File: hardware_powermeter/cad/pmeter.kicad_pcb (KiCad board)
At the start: 4 copper layers, 47 x 14 mm, 59 parts, among them J101 conector magnetico 6 vias, J102 furos da celula, J301 furos da ponte, U101 nPM1100-QDAB, U102 MAX17048G+T10, U201 HOLYIOT-26001-A, U301 ADS1220IRVAR, U302 TPS22916BYFPR, U401 BMA400, U402 TMP117AIDRVR

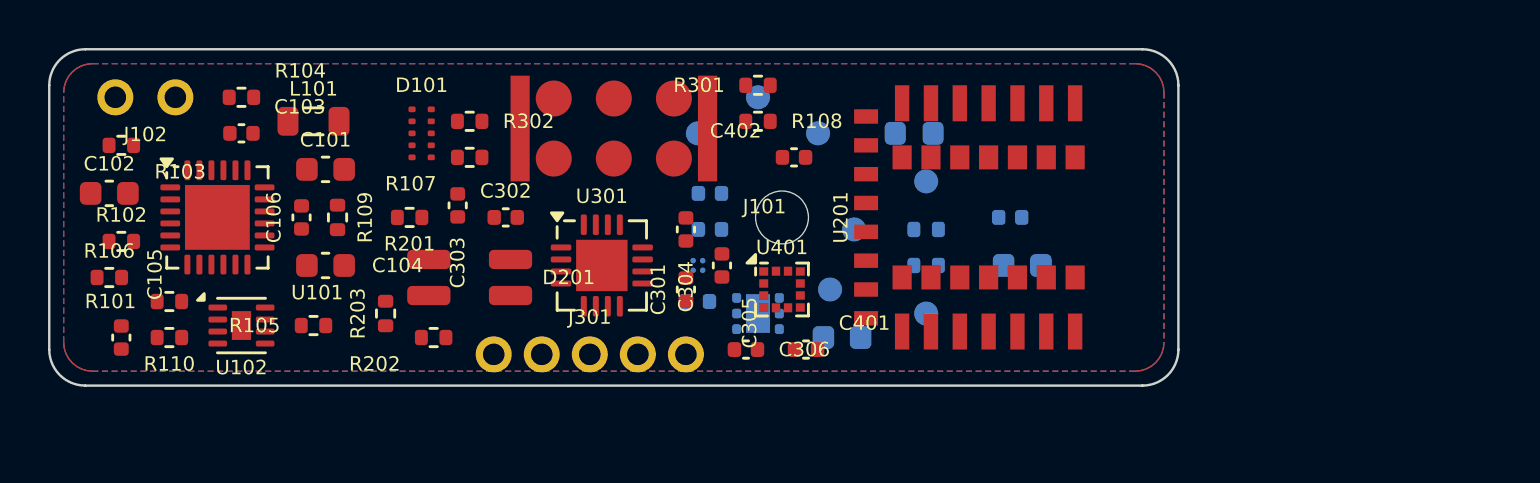
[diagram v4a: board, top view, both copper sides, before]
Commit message: feat(hardware): the board routed with zero DRC errors, and every view redrawn
The chain ran in its documented order for the first time since the module
swap -- make_pcb, route, fill_zones, drc, reparar, twice -- and the board
came out with 440 segments, 153 vias, 75 connections and NO DRC errors.
The 25 warnings are all library registration: the footprints here are
generated, not taken from a registered library.

What is still open, and the board cannot be fabricated until it closes:
three signal connections with no copper (I2C_SCL, SPI_MOSI, SPI_SCK, all
in the same stretch between the converter and the module), and seven of
seventeen decoupling capacitors past the datasheet limit. The second one
was measured from inside the placer rather than guessed: it decides
correctly, and the nearest FREE slot really is 2,90 mm from C302's pin.
What eats that radius is the stack of courtyards, so on a 3,5 mm VQFN
with a 0402 on the same face the datasheet's 2 mm may not fit at all.

The negotiated-congestion stage ran all 160 rounds and was refused: it
reaches zero contested cells only at 62 to 64 connections against the
sequential 75, and the criterion wants both.

Dry runs: 14 rules met on the board, 5 violated, 5 not measurable here;
17 met on the pod with one violated -- PD17, which is a requirement about
the BICYCLE and only a caliper can settle it.

All fifteen views, the board and assembly PDFs, the pod PDF and the two
STL are redrawn from this board. And the whole project's verification ran
three times with identical results.
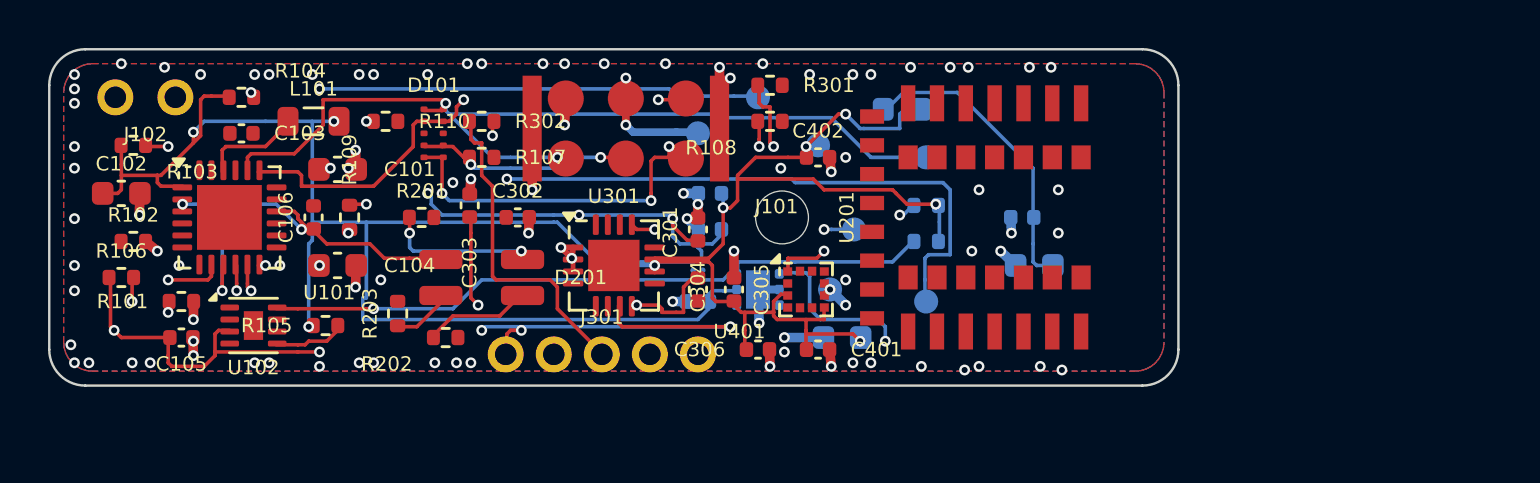
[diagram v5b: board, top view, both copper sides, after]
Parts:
- moved R110 12.7 mm to (39.0, 28.0)
- moved C105 2.50 mm to (30.5, 37.0), turned to 0 degrees
- moved C305 1.12 mm to (53.5, 35.0)
- moved FB201 1.12 mm to (60.5, 27.5)
- moved C402 1.00 mm to (57.0, 29.5)
- moved R204 1.00 mm to (61.5, 33.0)
- moved R205 1.00 mm to (61.5, 31.5)
- moved TP201 1.00 mm to (61.5, 29.5)
- moved U401 1.00 mm to (56.5, 35.0)
- moved U402 1.00 mm to (54.5, 35.0)
- moved C101 0.50 mm to (37.0, 30.0)
- moved C102 0.50 mm to (28.0, 31.0)
- moved C104 0.50 mm to (37.0, 34.0)
- moved C106 0.50 mm to (36.0, 32.0)
- moved C201 0.50 mm to (65.5, 32.0)
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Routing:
- net 3V0: track 0.00 -> 110.0 mm, vias 0 -> 9
- net 3V0_EXC: track 0.00 -> 59.1 mm, vias 0 -> 7
- net VBAT: track 0.00 -> 53.0 mm, vias 0 -> 4
- net UART_RX: track 0.00 -> 48.1 mm, vias 0 -> 3
- net UART_TX: track 0.00 -> 38.2 mm, vias 0 -> 2
- net I2C_SDA: track 0.00 -> 28.0 mm, vias 0 -> 1
- net GND: track 0.00 -> 26.1 mm, vias 0 -> 94
- net VBUS: track 0.00 -> 24.7 mm, vias 0 -> 4
- net AIN_N: track 0.00 -> 22.1 mm, vias 0 -> 3
- net SWCLK_J: track 0.00 -> 19.5 mm, vias 0 -> 4
- net BR_SP: track 0.00 -> 19.0 mm, vias 0 -> 1
- net VSYS: track 0.00 -> 18.6 mm, vias 0 -> 3
- net BR_SN: track 0.00 -> 13.5 mm
- net I2C_SCL: track 0.00 -> 13.0 mm, vias 0 -> 2
- net 3V0_MOD: track 0.00 -> 12.8 mm
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
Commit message: feat(hardware): the board with the radio module actually connected
Everything measured about routing before today measured a board where a
quarter of the connections did not exist. With the module's pads carrying
nets, the router has 25 more connections to make: 551 segments, 137 vias,
81 connections, still ZERO DRC errors, and 30 unconnected items against
the old 14 -- that 14 was flattering by omission.

Of the 49 the router did not close, 22 are ground stitching vias the pour
resolves. The signal ones cluster in two places and both are fine-pitch
pad escape: the nPM1100's pins, a 0,5 mm QFN with nine nets stuck at it,
and the module's. It is not area -- growing the board to 50 or 52 mm was
measured and gives 33 unconnected instead of 30.

Board dry run: 16 rules met, 4 violated, 4 not measurable. Pod dry run:
17 met, 1 violated, and that one is PD17, a requirement about the bicycle.
All fifteen views, both board PDFs, the pod PDF and the two STL are
redrawn from this board, and the whole project's verification ran three
times with identical results under the stricter board check.
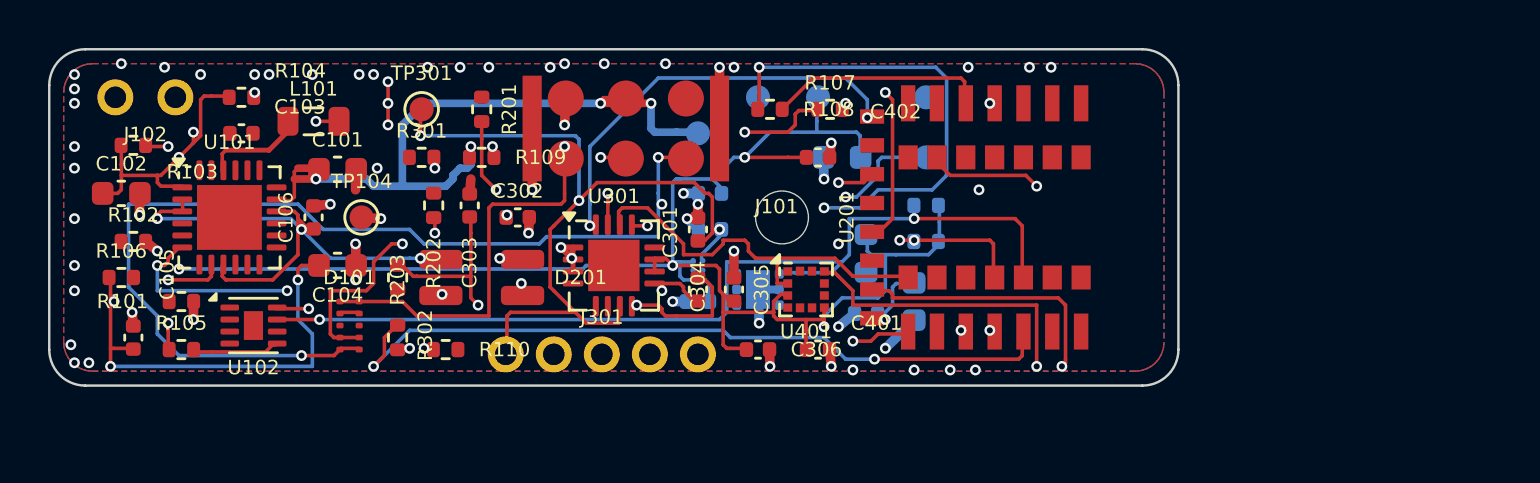
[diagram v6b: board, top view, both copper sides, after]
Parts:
- TP104, TP301: moved to F.Cu
- moved TP104 19.7 mm to (38.0, 32.0)
- moved TP301 18.7 mm to (40.5, 27.5)
- moved R301 14.8 mm to (40.5, 29.5)
- moved R107 14.6 mm to (57.5, 27.5)
- moved R110 9.82 mm to (41.5, 37.5)
- moved D101 8.73 mm to (37.5, 36.5)
- moved TP202 8.50 mm to (61.5, 27.0)
- moved C201 7.63 mm to (59.0, 36.0)
- moved C203 7.50 mm to (58.0, 29.5)
- moved R302 7.38 mm to (39.5, 34.5), turned to 90 degrees
- moved FB201 6.18 mm to (59.0, 33.5), turned to 90 degrees
- moved R105 6.08 mm to (30.5, 37.5)
- moved R109 6.04 mm to (43.0, 29.5), turned to 0 degrees
- moved R202 5.52 mm to (41.0, 31.5), turned to 90 degrees
- moved C202 5.22 mm to (61.0, 35.5), turned to 90 degrees
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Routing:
- net VBUS_SENSE: track 4.50 -> 76.1 mm, vias 2 -> 6
- net SWCLK_J: track 19.5 -> 71.7 mm, vias 4 -> 5
- net SHPACT: track 0.00 -> 49.9 mm, vias 0 -> 3
- net UART_RX: track 48.1 -> 0.75 mm, vias 3 -> 0
- net LED_B: track 0.00 -> 31.4 mm, vias 0 -> 2
- net I2C_SCL: track 13.0 -> 40.5 mm
- net VBAT: track 53.0 -> 27.0 mm, vias 4 -> 3
- net 3V0_EXC: track 59.1 -> 33.6 mm, vias 7 -> 3
- net IMU_CS: track 0.00 -> 24.6 mm, vias 0 -> 2
- net SWDIO_J: track 9.13 -> 32.4 mm, vias 2 -> 3
- net ERR_N: track 9.76 -> 32.9 mm
- net BR_SP: track 19.0 -> 0.00 mm, vias 1 -> 0
- net AIN_P: track 0.00 -> 18.8 mm, vias 0 -> 3
- net ADC_CS: track 0.00 -> 17.6 mm, vias 0 -> 2
- net SPI_MOSI: track 0.00 -> 16.4 mm
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
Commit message: feat(cad): accept the negotiated routing and clean it, and the board closes
The negotiated-congestion stage had never once been accepted. Its
criterion demanded ZERO contested cells, and on this board it reaches zero
only at 62 to 64 connections against the sequential router's 81 -- so
every run spent forty minutes on it and threw the answer away.

The geometric cleanup built earlier today changes that: it removes the
offending track and the offending via one at a time until the board is
clean. So the negotiated answer can be accepted and cleaned afterwards.
It closes in 25 rounds with 88 connections and zero contested cells, and
the board goes from 551 to 1383 segments, from 81 to 88 connections, and
from 30 to 21 unconnected items, still with ZERO DRC errors. Of the 44
the router did not close, every one belongs to a single net -- the ground
plane's stitching -- against 23 nets before.

And the best-round criterion has to be the CLEANEST, not the fullest.
Changed to prefer more connections, the stage picked a round with 107
connections and 240 pairs too close; the cleanup removed 40 tracks and
stopped, and the DRC reported 217 errors. Measured both ways before
deciding.

Board dry run: 15 rules met, 5 violated, 4 not measurable. Pod dry run:
17 met, 1 violated (PD17, the requirement about the bicycle). check_pcb
is down to one failure, overlapping silkscreen. Every drawing is redrawn
from this board and the whole verification ran three times identically.
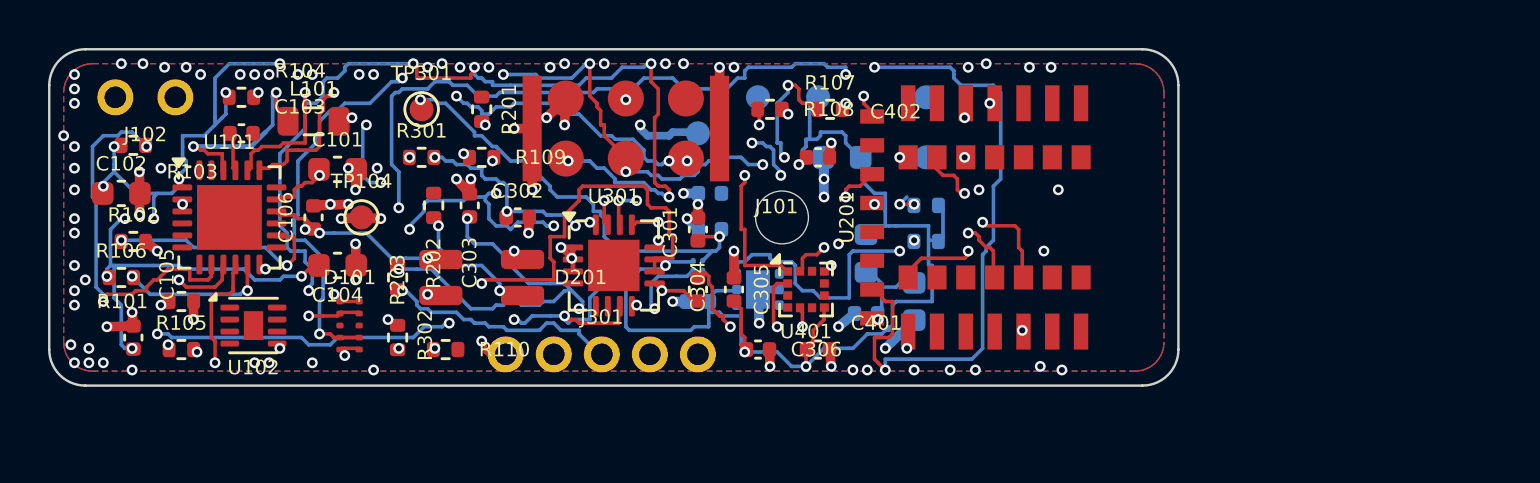
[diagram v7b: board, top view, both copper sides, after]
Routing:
- net SHPACT: track 49.9 -> 0.00 mm, vias 3 -> 0
- net SWCLK_J: track 71.7 -> 32.8 mm, vias 5 -> 7
- net I2C_SCL: track 40.5 -> 8.08 mm, vias 2 -> 3
- net EXC_EN: track 0.00 -> 27.8 mm, vias 0 -> 2
- net UART_RX: track 0.75 -> 24.7 mm, vias 0 -> 2
- net SPI_MISO: track 15.9 -> 37.7 mm, vias 2 -> 5
- net I2C_SDA: track 35.8 -> 16.2 mm
- net LED_B: track 31.4 -> 49.0 mm, vias 2 -> 4
- net VBUS_SENSE: track 76.1 -> 59.9 mm, vias 6 -> 7
- net ADC_DRDY: track 0.00 -> 14.5 mm, vias 0 -> 2
- net 3V0: track 94.1 -> 107.7 mm, vias 8 -> 15
- net IMU_CS: track 24.6 -> 11.0 mm
- net BR_SP: track 0.00 -> 12.7 mm, vias 0 -> 1
- net ERR_N: track 32.9 -> 21.2 mm
- net SPI_MOSI: track 16.4 -> 27.7 mm, vias 0 -> 4
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
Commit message: feat(hardware): route the board with the finer rules, and shorten the placement
The board now carries 93 routed connections, 651 tracks and 217 vias with
ZERO DRC errors, against 75 connections and 440 tracks before. Twenty-one
connections are still open and the drawings say so.

The placement gained an improvement pass. The placer was constructive -
anchors, decoupling against the pin, the rest by waves of connectivity -
and nobody looked at the result afterwards. The new pass does what a
person does at the end: each movable part tries other spots nearby and
keeps whatever shortens the half-perimeter of the nets it is on. It takes
31.8 mm of connection off the board, and it is what let the negotiated
stage close at all.

It costs something, and the cost is measured rather than argued: loose,
the decoupling is pulled toward the centre of its nets and AL1 goes from
7 of 17 capacitors out of limit (3.06 mm average) to 11 of 19 (3.85 mm).
Frozen, the gain drops to 3.5 mm; on a 2 mm leash, to 5.8 mm; in both
cases the negotiation fails and the board falls back to 85 connections.
It stays loose. AL1 remains the grave item it already was - it does not
get solved by moving parts, but by more area, which the board does not
have.

Silkscreen labels are now kept per face, because F.SilkS and B.SilkS are
two different prints, and the candidate ring goes out to 4 mm in finer
steps. Three overlapping designators became one, and that one is recorded
rather than hidden.

What was tried and measured as WORSE, so it is not here: an escape
reservation around every pad (20 to 30 unconnected), ground stitching in
the repair pass (26 DRC errors, 14 of them hole near hole), the ADS1220
block on the back face (one part off the board, three resistors carried
14 to 25 mm, 93 connections down to 90), and a physical escape ring around
the nPM1100 (six parts off the board, nothing closed).
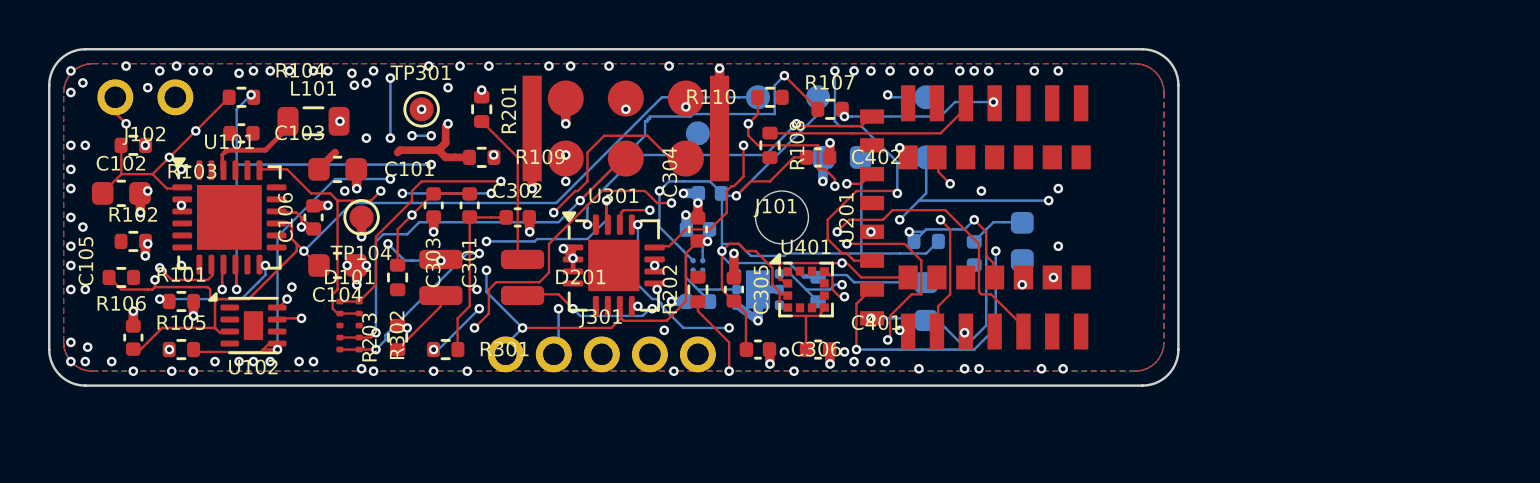
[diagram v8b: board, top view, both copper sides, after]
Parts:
- moved R110 17.1 mm to (55.0, 27.0)
- moved R202 11.5 mm to (52.0, 35.0)
- moved C301 10.1 mm to (42.5, 31.5)
- moved R301 8.06 mm to (41.5, 37.5)
- moved R205 5.70 mm to (57.0, 35.0), turned to 90 degrees
- moved C201 5.15 mm to (63.5, 33.5), turned to 90 degrees
- moved C202 5.15 mm to (65.5, 33.0)
- moved FB201 3.20 mm to (61.5, 35.5)
- moved C303 1.50 mm to (41.0, 31.5), turned to -90 degrees
- moved R108 1.50 mm to (55.0, 29.0), turned to 90 degrees
- moved C307 0.50 mm to (52.0, 32.5)
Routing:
- net GAUGE_ALRT: track 3.94 -> 50.8 mm, vias 2 -> 6
- net UART_RX: track 24.7 -> 57.8 mm, vias 2 -> 4
- net LED_R: track 0.00 -> 31.0 mm, vias 0 -> 2
- net LED_KG: track 5.87 -> 34.2 mm, vias 2 -> 5
- net EXC_EN: track 27.8 -> 0.00 mm, vias 2 -> 0
- net I2C_SCL: track 8.08 -> 35.5 mm
- net VBAT: track 21.5 -> 48.2 mm, vias 4 -> 3
- net I2C_SDA: track 16.2 -> 42.7 mm, vias 3 -> 5
- net SPI_MISO: track 37.7 -> 15.0 mm, vias 5 -> 3
- net VBUS_SENSE: track 59.9 -> 38.9 mm, vias 7 -> 5
- net ERR_N: track 21.2 -> 38.3 mm, vias 2 -> 4
- net LED_B: track 49.0 -> 35.3 mm
- net SWCLK_J: track 32.8 -> 19.3 mm, vias 7 -> 3
- net SWDIO_J: track 42.4 -> 31.0 mm, vias 8 -> 3
- net GND: track 35.2 -> 24.0 mm, vias 99 -> 115
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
